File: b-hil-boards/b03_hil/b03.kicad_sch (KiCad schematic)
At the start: 48 parts, among them J1 Conn_01x20_Socket, J2 Conn_01x14_Socket, K1 Relay_DPDT, K2 Relay_DPDT, K3 Relay_DPDT, K4 Relay_DPDT, K5 Relay_DPDT, K6 Relay_DPDT, SW1 SW_Push, U1 74LVC2G34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

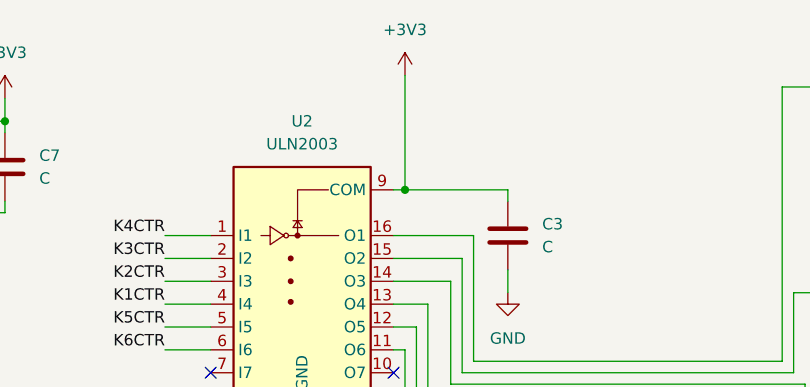
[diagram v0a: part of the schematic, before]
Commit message: B03: route all board traces
- Complete trace routing for B03 HIL board
- Update PCB layout (b03.kicad_pcb) and schematic (b03.kicad_sch)
- Add routing session/export files and backups
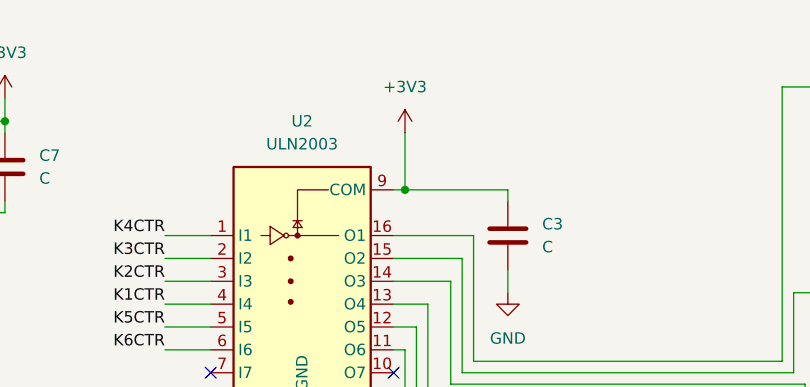
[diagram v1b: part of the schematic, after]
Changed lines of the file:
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@@
     (stroke (width 0) (type default))
   )
-  (wire (pts (xy 142.24 29.21) (xy 142.24 16.51))
+  (wire (pts (xy 142.24 29.21) (xy 142.24 22.86))
     (stroke (width 0) (type default))
   )
@@
     )
   )
-  (symbol (lib_id "power:+3V3") (at 142.24 16.51 0) (unit 1)
-    (in_bom yes) (on_board yes) (dnp no) (fields_autoplaced)
-    (property "Reference" "#PWR016" (at 142.24 20.32 0)
-      (effects (font (size 1.27 1.27)) hide)
-    )
-    (property "Value" "+3V3" (at 142.24 11.43 0)
-      (effects (font (size 1.27 1.27)))
-    )
-    (property "Footprint" "" (at 142.24 16.51 0)
-      (effects (font (size 1.27 1.27)) hide)
-    )
-    (property "Datasheet" "" (at 142.24 16.51 0)
-      (effects (font (size 1.27 1.27)) hide)
-    )
+  (symbol (lib_id "power:+3V3") (at 142.24 22.86 0) (unit 1)
+    (in_bom yes) (on_board yes) (dnp no) (fields_autoplaced)
+    (property "Reference" "#PWR016" (at 142.24 26.67 0)
+      (effects (font (size 1.27 1.27)) hide)
+    )
+    (property "Value" "+3V3" (at 142.24 17.78 0)
+      (effects (font (size 1.27 1.27)))
+    )
+    (property "Footprint" "" (at 142.24 22.86 0)
+      (effects (font (size 1.27 1.27)) hide)
+    )
+    (property "Datasheet" "" (at 142.24 22.86 0)
+      (effects (font (size 1.27 1.27)) hide)
+    )

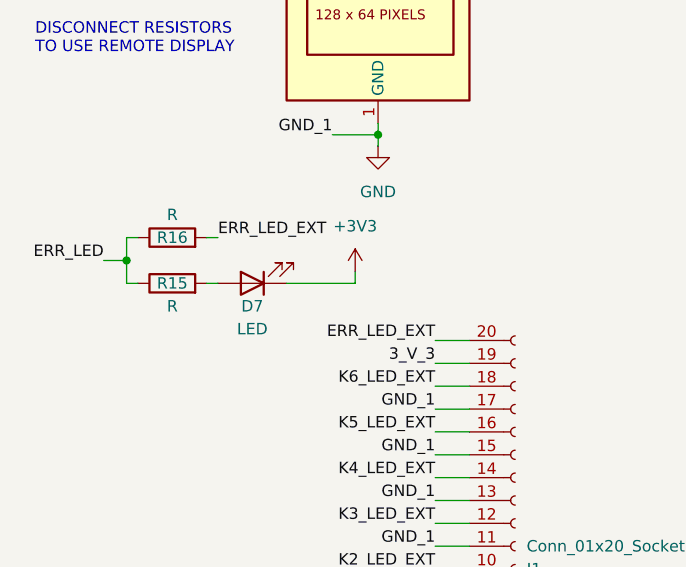
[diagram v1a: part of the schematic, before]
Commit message: fix(b03): correct LED D7 polarity on schematic and PCB
Fix reversed polarity marking/connection for D7 in b03.kicad_sch and
b03.kicad_pcb.
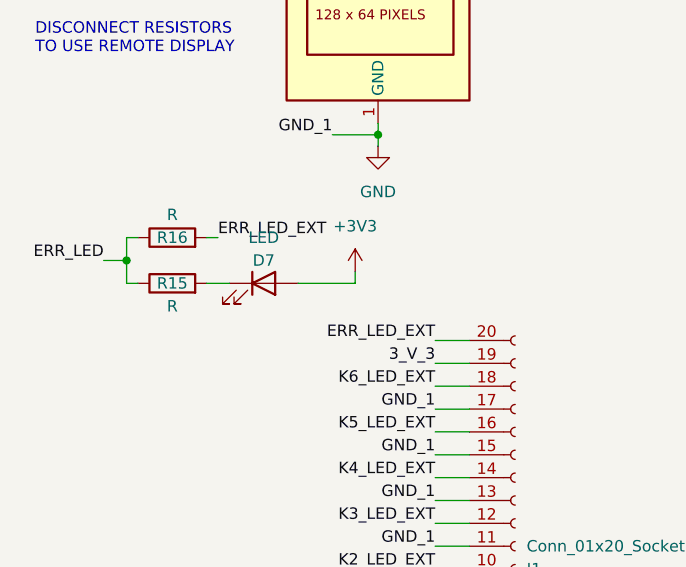
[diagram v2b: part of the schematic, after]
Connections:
- net +3V3: now also D7.2 (A); no longer D7.1 (K)
- net at R15.2: now also D7.1 (K); no longer D7.2 (A)
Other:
- moved on the sheet: D7
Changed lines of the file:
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@@
-    (stroke (width 0) (type default))
-  )
-  (wire (pts (xy 33.02 138.43) (xy 34.29 138.43))
     (stroke (width 0) (type default))
   )
@@
     (stroke (width 0) (type default))
   )
+  (wire (pts (xy 43.18 138.43) (xy 49.53 138.43))
+    (stroke (width 0) (type default))
+  )
   (wire (pts (xy 148.59 90.17) (xy 149.86 90.17))
     (stroke (width 0) (type default))
@@
     (stroke (width 0) (type default))
   )
-  (wire (pts (xy 41.91 138.43) (xy 49.53 138.43))
-    (stroke (width 0) (type default))
-  )
   (wire (pts (xy 104.14 162.56) (xy 104.14 163.83))
     (stroke (width 0) (type default))
@@
   )
   (wire (pts (xy 157.48 167.64) (xy 161.29 167.64))
+    (stroke (width 0) (type default))
+  )
+  (wire (pts (xy 33.02 138.43) (xy 35.56 138.43))
     (stroke (width 0) (type default))
   )
@@
     )
   )
-  (symbol (lib_id "Device:LED") (at 38.1 138.43 180) (unit 1)
-    (in_bom yes) (on_board yes) (dnp no)
-    (property "Reference" "D7" (at 38.1 140.97 0)
-      (effects (font (size 1.27 1.27)))
-    )
-    (property "Value" "LED" (at 38.1 143.51 0)
-      (effects (font (size 1.27 1.27)))
-    )
-    (property "Footprint" "LED_SMD:LED_0805_2012Metric_Pad1.15x1.40mm_HandSolder" (at 38.1 138.43 0)
-      (effects (font (size 1.27 1.27)) hide)
-    )
-    (property "Datasheet" "~" (at 38.1 138.43 0)
-      (effects (font (size 1.27 1.27)) hide)
-    )
+  (symbol (lib_id "Device:LED") (at 39.37 138.43 0) (unit 1)
+    (in_bom yes) (on_board yes) (dnp no)
+    (property "Reference" "D7" (at 39.37 135.89 0)
+      (effects (font (size 1.27 1.27)))
+    )
+    (property "Value" "LED" (at 39.37 133.35 0)
+      (effects (font (size 1.27 1.27)))
+    )
+    (property "Footprint" "LED_SMD:LED_0805_2012Metric_Pad1.15x1.40mm_HandSolder" (at 39.37 138.43 0)
+      (effects (font (size 1.27 1.27)) hide)
+    )
+    (property "Datasheet" "~" (at 39.37 138.43 0)
+      (effects (font (size 1.27 1.27)) hide)
+    )

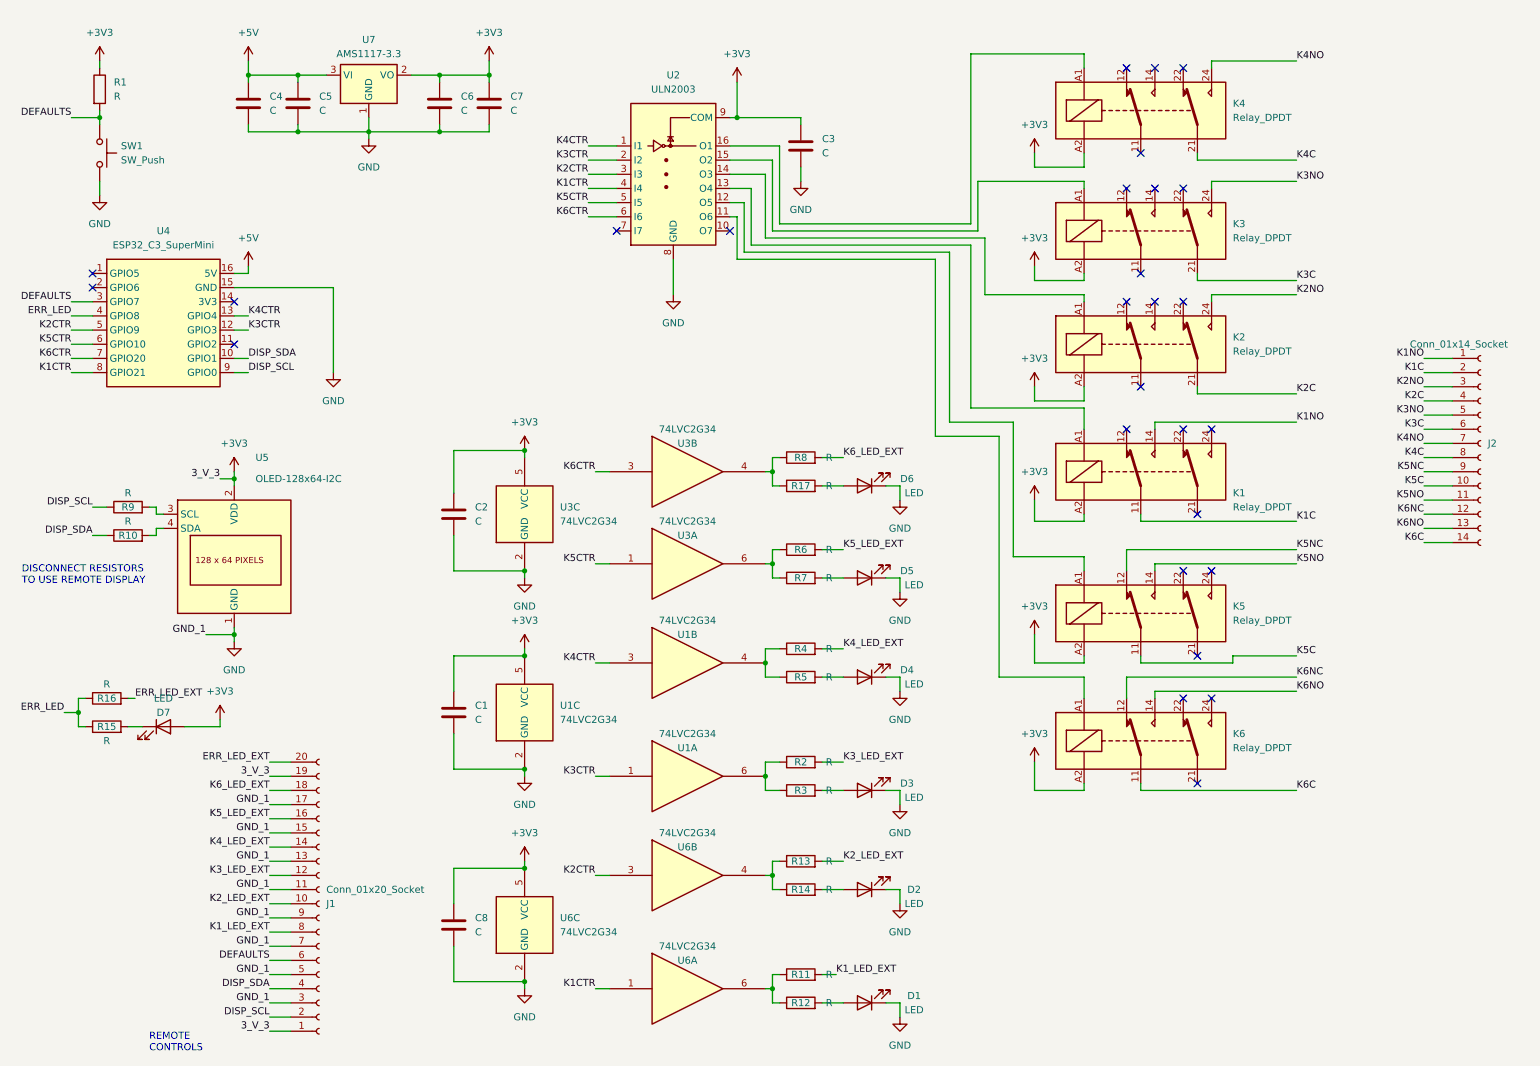
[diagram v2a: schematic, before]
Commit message: B03: add tri-state buffer and re-route PCB
Add 74HCT541 tri-state buffer to the schematic and re-route b03.kicad_pcb
to integrate the new device. Update project settings, replace FreeRouting
exchange files (b03.dsn, b03.rules, b03.ses; remove legacy b02.*), and
rotate KiCad automatic backup archives.
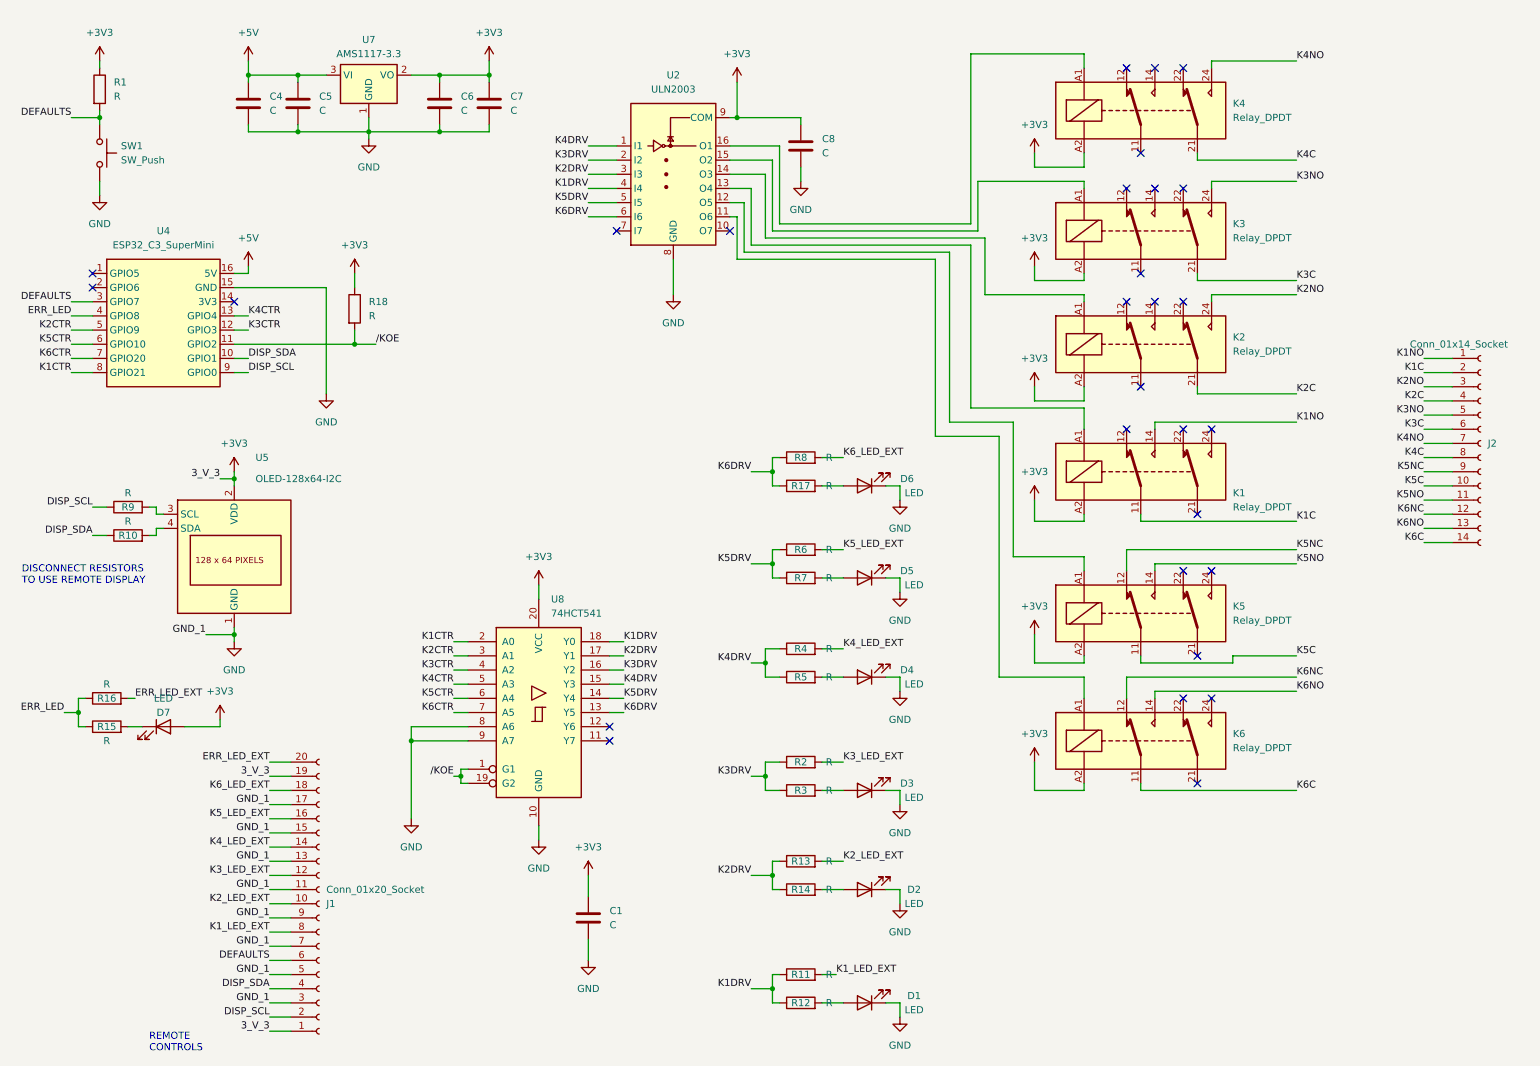
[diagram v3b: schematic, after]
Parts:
- removed C2, C8: C, Capacitor_SMD:C_0805_2012Metric_Pad1.18x1.45mm_HandSolder, symbol Device:C
- removed U1, U3, U6: 74LVC2G34, Package_TO_SOT_SMD:SOT-23-6_Handsoldering, symbol 74xGxx:74LVC2G34
- added R18: R, Resistor_SMD:R_0805_2012Metric_Pad1.20x1.40mm_HandSolder, symbol Device:R
- added U8: 74HCT541, Package_SO:TSSOP-20_4.4x6.5mm_P0.65mm, symbol 74xx:74HCT541
- renumbered C3 to C8
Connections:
- net +3V3: now also R18.1, U8.20 (VCC)
- net GND: now also U8.10 (GND), U8.8 (A6), U8.9 (A7)
- net K1CTR: now also U8.2 (A0); no longer U2.4 (I4)
- net K2CTR: now also U8.3 (A1); no longer U2.3 (I3)
- net K3CTR: now also U8.4 (A2); no longer U2.2 (I2)
- net K4CTR: now also U8.5 (A3); no longer U2.1 (I1)
- net K5CTR: now also U8.6 (A4); no longer U2.5 (I5)
- net K6CTR: now also U8.7 (A5); no longer U2.6 (I6)
- net K6DRV: now reaches R17.1, R8.1
- net K6DRV: now also U2.6 (I6), U8.13 (Y5)
- net K4DRV: now reaches R4.1, R5.1
- net K4DRV: now also U2.1 (I1), U8.15 (Y3)
- net K3DRV: now reaches R2.1, R3.1
- net K3DRV: now also U2.2 (I2), U8.16 (Y2)
- net K5DRV: now reaches R6.1, R7.1
- net K5DRV: now also U2.5 (I5), U8.14 (Y4)
- net K2DRV: now reaches R13.1, R14.1
- net K2DRV: now also U2.3 (I3), U8.17 (Y1)
- net /KOE: now reaches U4.11 (GPIO2)
- net /KOE: now also R18.2, U8.1 (G1), U8.19 (G2)
- net K1DRV: now reaches R11.1, R12.1
- net K1DRV: now also U2.4 (I4), U8.18 (Y0)
- no-connect marks 28 -> 29
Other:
- moved on the sheet: C1
